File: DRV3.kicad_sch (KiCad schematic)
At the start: 15 parts

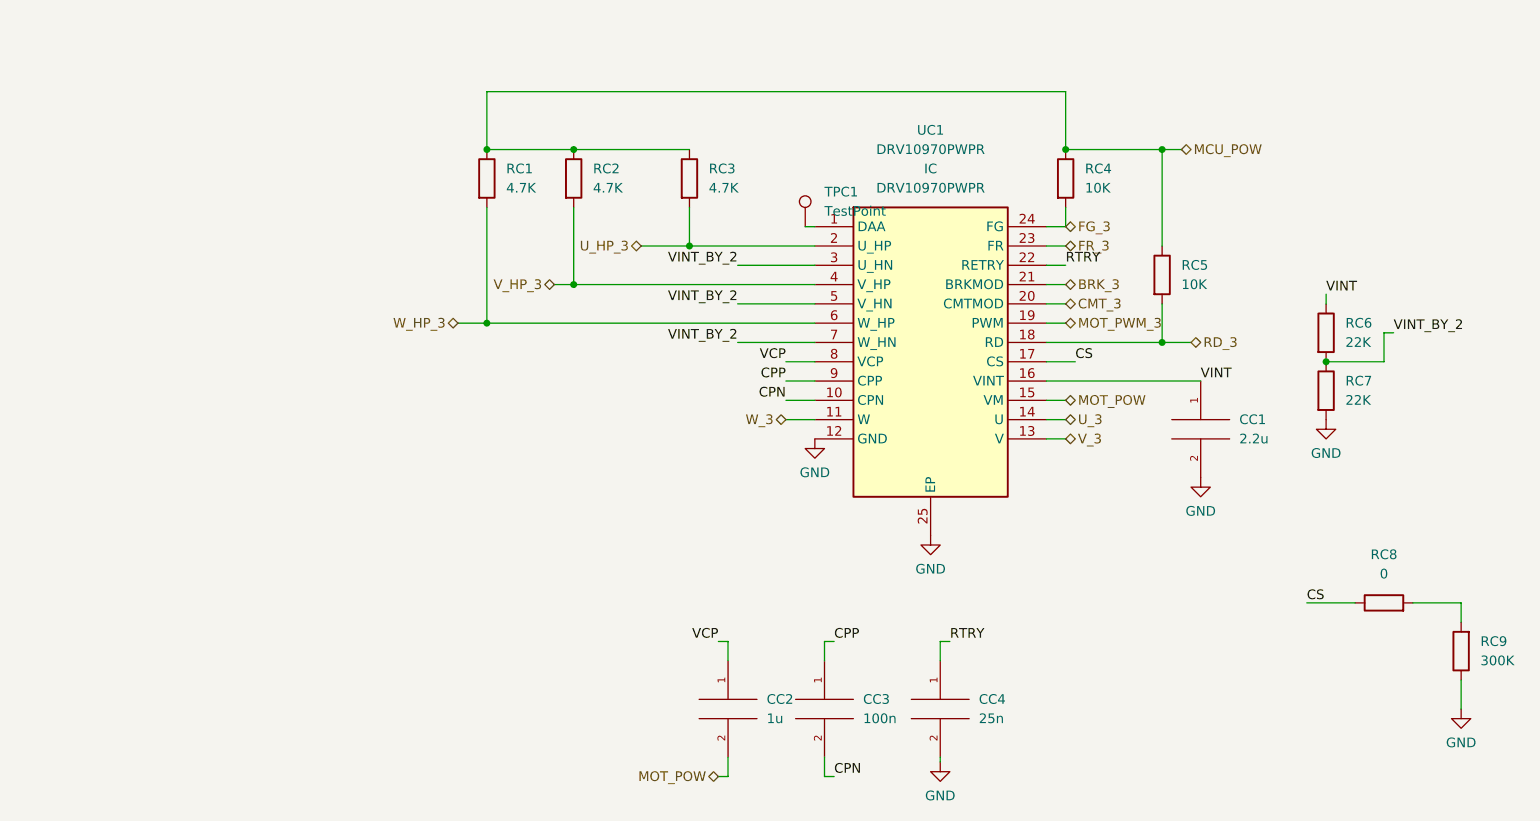
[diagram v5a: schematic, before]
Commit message: Page settings changed. Added some testpoints. Some comments are made.
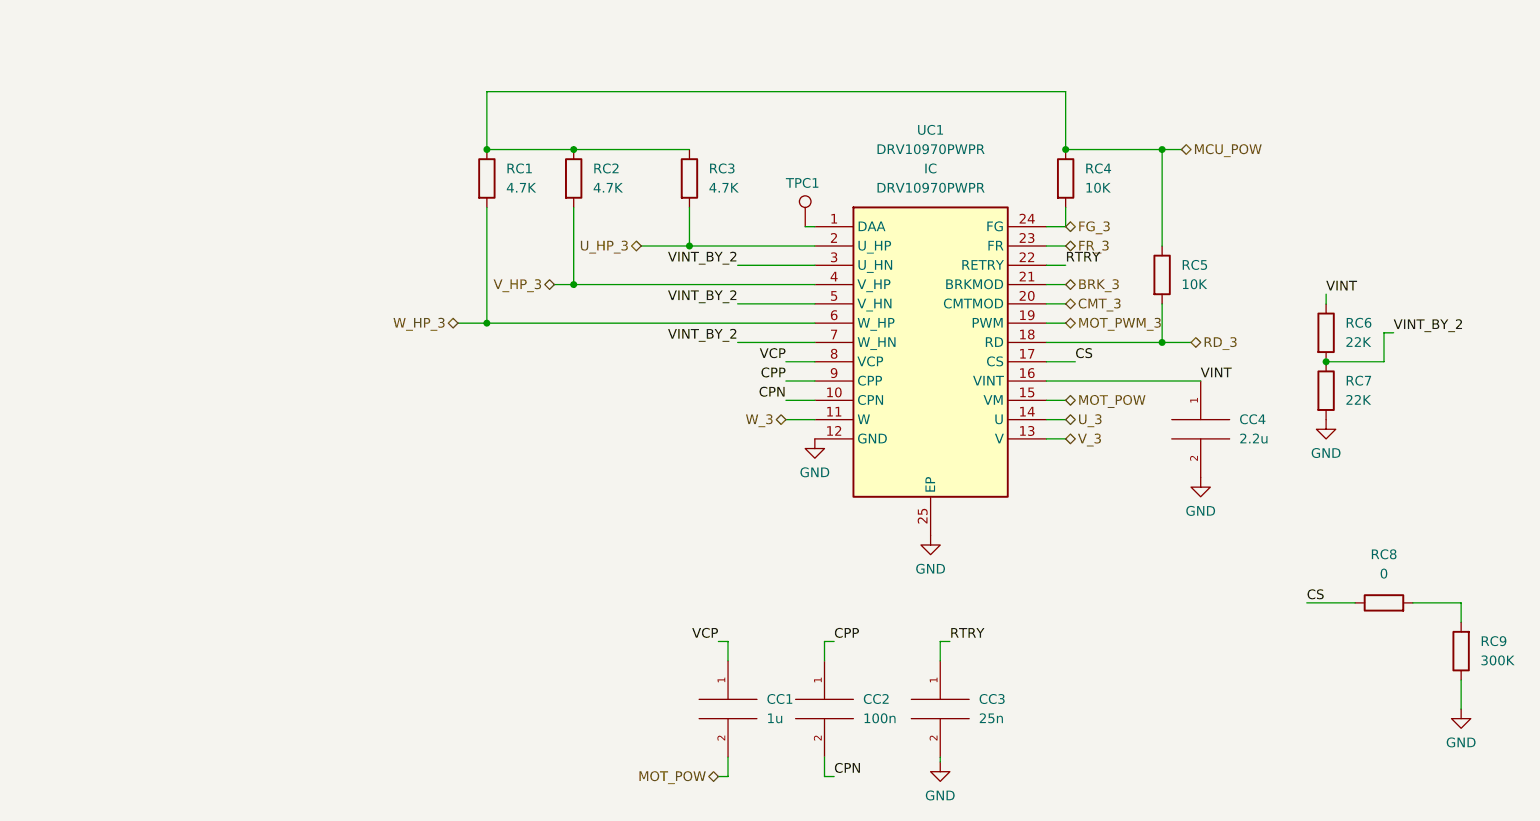
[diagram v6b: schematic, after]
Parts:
- TPC1: footprint (none) -> TestPoint:TestPoint_Plated_Hole_D2.0mm
- renumbered CC2 to CC1, CC3 to CC2, CC4 to CC3, CC1 to CC4
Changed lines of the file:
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@@
   (symbol (lib_id "upsat-comms-hardware:GND") (at 181.61 109.22 0) (unit 1)
     (in_bom yes) (on_board yes) (fields_autoplaced)
-    (property "Reference" "#PWR093" (id 0) (at 181.61 115.57 0)
+    (property "Reference" "#PWR0107" (id 0) (at 181.61 115.57 0)
       (effects (font (size 1.27 1.27)) hide)
     )
@@
   (symbol (lib_id "upsat-comms-hardware:GND") (at 130.81 104.14 0) (unit 1)
     (in_bom yes) (on_board yes) (fields_autoplaced)
-    (property "Reference" "#PWR092" (id 0) (at 130.81 110.49 0)
+    (property "Reference" "#PWR0104" (id 0) (at 130.81 110.49 0)
       (effects (font (size 1.27 1.27)) hide)
     )
@@
   (symbol (lib_id "pspice:C") (at 132.08 139.7 0) (unit 1)
     (in_bom yes) (on_board yes) (fields_autoplaced)
-    (property "Reference" "CC3" (id 0) (at 137.16 138.4299 0)
+    (property "Reference" "CC2" (id 0) (at 137.16 138.4299 0)
       (effects (font (size 1.27 1.27)) (justify left))
     )
@@
   (symbol (lib_id "upsat-comms-hardware:GND") (at 215.9 139.7 0) (unit 1)
     (in_bom yes) (on_board yes) (fields_autoplaced)
-    (property "Reference" "#PWR095" (id 0) (at 215.9 146.05 0)
+    (property "Reference" "#PWR0109" (id 0) (at 215.9 146.05 0)
       (effects (font (size 1.27 1.27)) hide)
     )
@@
     (pin "1")
   )
+  (symbol (lib_id "Connector:TestPoint") (at 129.54 76.2 0) (unit 1)
+    (in_bom yes) (on_board yes)
+    (property "Reference" "TPC1" (id 0) (at 127 70.485 0)
+      (effects (font (size 1.27 1.27)) (justify left))
+    )
+    (property "Value" "TestPoint" (id 1) (at 125.095 70.485 0)
+      (effects (font (size 1.27 1.27)) (justify left) hide)
+    )
+    (property "Footprint" "TestPoint:TestPoint_Plated_Hole_D2.0mm" (id 2) (at 134.62 76.2 0)
+      (effects (font (size 1.27 1.27)) hide)
+    )
+    (property "Datasheet" "~" (id 3) (at 134.62 76.2 0)
+      (effects (font (size 1.27 1.27)) hide)
+    )
+    (pin "1")
+  )
   (symbol (lib_id "pspice:C") (at 147.32 139.7 0) (unit 1)
     (in_bom yes) (on_board yes) (fields_autoplaced)
-    (property "Reference" "CC4" (id 0) (at 152.4 138.4299 0)
+    (property "Reference" "CC3" (id 0) (at 152.4 138.4299 0)
       (effects (font (size 1.27 1.27)) (justify left))
     )
@@
   (symbol (lib_id "pspice:C") (at 119.38 139.7 0) (unit 1)
     (in_bom yes) (on_board yes) (fields_autoplaced)
-    (property "Reference" "CC2" (id 0) (at 124.46 138.4299 0)
+    (property "Reference" "CC1" (id 0) (at 124.46 138.4299 0)
       (effects (font (size 1.27 1.27)) (justify left))
     )
@@
   (symbol (lib_id "upsat-comms-hardware:GND") (at 146.05 116.84 0) (unit 1)
     (in_bom yes) (on_board yes) (fields_autoplaced)
-    (property "Reference" "#PWR094" (id 0) (at 146.05 123.19 0)
+    (property "Reference" "#PWR0105" (id 0) (at 146.05 123.19 0)
       (effects (font (size 1.27 1.27)) hide)
     )
@@
   (symbol (lib_id "upsat-comms-hardware:GND") (at 198.12 101.6 0) (unit 1)
     (in_bom yes) (on_board yes) (fields_autoplaced)
-    (property "Reference" "#PWR091" (id 0) (at 198.12 107.95 0)
+    (property "Reference" "#PWR0108" (id 0) (at 198.12 107.95 0)
       (effects (font (size 1.27 1.27)) hide)
     )
@@
   (symbol (lib_id "upsat-comms-hardware:GND") (at 147.32 146.685 0) (unit 1)
     (in_bom yes) (on_board yes) (fields_autoplaced)
-    (property "Reference" "#PWR096" (id 0) (at 147.32 153.035 0)
+    (property "Reference" "#PWR0106" (id 0) (at 147.32 153.035 0)
       (effects (font (size 1.27 1.27)) hide)
     )
@@
     (property "Footprint" "" (id 2) (at 147.32 146.685 0))
     (property "Datasheet" "" (id 3) (at 147.32 146.685 0))
-    (pin "1")
-  )
-  (symbol (lib_id "Connector:TestPoint") (at 129.54 76.2 0) (unit 1)
-    (in_bom yes) (on_board yes) (fields_autoplaced)
-    (property "Reference" "TPC1" (id 0) (at 132.08 71.6279 0)
-      (effects (font (size 1.27 1.27)) (justify left))
-    )
-    (property "Value" "TestPoint" (id 1) (at 132.08 74.1679 0)
-      (effects (font (size 1.27 1.27)) (justify left))
-    )
-    (property "Footprint" "" (id 2) (at 134.62 76.2 0)
-      (effects (font (size 1.27 1.27)) hide)
-    )
-    (property "Datasheet" "~" (id 3) (at 134.62 76.2 0)
-      (effects (font (size 1.27 1.27)) hide)
-    )
     (pin "1")
   )
@@
   (symbol (lib_id "pspice:C") (at 181.61 102.87 0) (unit 1)
     (in_bom yes) (on_board yes) (fields_autoplaced)
-    (property "Reference" "CC1" (id 0) (at 186.69 101.5999 0)
-      (effects (font (size 1.27 1.27)) (justify left))
-    )
+    (property "Reference" "CC4" (id 0) (at 186.69 101.5999 0)
+      (effects (font (size 1.27 1.27)) (justify left))
+    )

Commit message: I2C lines are pulled up
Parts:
- CC1, CC2, CC3, CC4: footprint (none) -> Capacitor_SMD:C_0603_1608Metric
- RC1, RC2, RC3, RC4, RC5, RC6, RC7, RC8, RC9: footprint (none) -> Resistor_SMD:R_0603_1608Metric
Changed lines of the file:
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@@
     (property "Reference" "RC8" (id 0) (at 205.74 119.38 90))
     (property "Value" "0" (id 1) (at 205.74 121.92 90))
-    (property "Footprint" "" (id 2) (at 205.74 127.508 90)
+    (property "Footprint" "Resistor_SMD:R_0603_1608Metric" (id 2) (at 205.74 127.508 90)
       (effects (font (size 1.27 1.27)) hide)
     )
@@
       (effects (font (size 1.27 1.27)) (justify left))
     )
-    (property "Footprint" "" (id 2) (at 174.752 82.55 90)
+    (property "Footprint" "Resistor_SMD:R_0603_1608Metric" (id 2) (at 174.752 82.55 90)
       (effects (font (size 1.27 1.27)) hide)
     )
@@
       (effects (font (size 1.27 1.27)) (justify left))
     )
-    (property "Footprint" "" (id 2) (at 162.052 69.85 90)
+    (property "Footprint" "Resistor_SMD:R_0603_1608Metric" (id 2) (at 162.052 69.85 90)
       (effects (font (size 1.27 1.27)) hide)
     )
@@
       (effects (font (size 1.27 1.27)) (justify left))
     )
-    (property "Footprint" "" (id 2) (at 97.282 69.85 90)
+    (property "Footprint" "Resistor_SMD:R_0603_1608Metric" (id 2) (at 97.282 69.85 90)
       (effects (font (size 1.27 1.27)) hide)
     )
@@
   (symbol (lib_id "upsat-comms-hardware:GND") (at 181.61 109.22 0) (unit 1)
     (in_bom yes) (on_board yes) (fields_autoplaced)
-    (property "Reference" "#PWR0107" (id 0) (at 181.61 115.57 0)
+    (property "Reference" "#PWR0108" (id 0) (at 181.61 115.57 0)
       (effects (font (size 1.27 1.27)) hide)
     )
@@
       (effects (font (size 1.27 1.27)) (justify right))
     )
-    (property "Footprint" "" (id 2) (at 217.678 132.08 90)
+    (property "Footprint" "Resistor_SMD:R_0603_1608Metric" (id 2) (at 217.678 132.08 90)
       (effects (font (size 1.27 1.27)) hide)
     )
@@
   (symbol (lib_id "upsat-comms-hardware:GND") (at 130.81 104.14 0) (unit 1)
     (in_bom yes) (on_board yes) (fields_autoplaced)
-    (property "Reference" "#PWR0104" (id 0) (at 130.81 110.49 0)
+    (property "Reference" "#PWR0105" (id 0) (at 130.81 110.49 0)
       (effects (font (size 1.27 1.27)) hide)
     )
@@
       (effects (font (size 1.27 1.27)) (justify left))
     )
-    (property "Footprint" "" (id 2) (at 112.522 69.85 90)
+    (property "Footprint" "Resistor_SMD:R_0603_1608Metric" (id 2) (at 112.522 69.85 90)
       (effects (font (size 1.27 1.27)) hide)
     )
@@
       (effects (font (size 1.27 1.27)) (justify left))
     )
-    (property "Footprint" "" (id 2) (at 132.08 139.7 0)
+    (property "Footprint" "Capacitor_SMD:C_0603_1608Metric" (id 2) (at 132.08 139.7 0)
       (effects (font (size 1.27 1.27)) hide)
     )
@@
   (symbol (lib_id "upsat-comms-hardware:GND") (at 215.9 139.7 0) (unit 1)
     (in_bom yes) (on_board yes) (fields_autoplaced)
-    (property "Reference" "#PWR0109" (id 0) (at 215.9 146.05 0)
+    (property "Reference" "#PWR0110" (id 0) (at 215.9 146.05 0)
       (effects (font (size 1.27 1.27)) hide)
     )
@@
       (effects (font (size 1.27 1.27)) (justify left))
     )
-    (property "Footprint" "" (id 2) (at 147.32 139.7 0)
+    (property "Footprint" "Capacitor_SMD:C_0603_1608Metric" (id 2) (at 147.32 139.7 0)
       (effects (font (size 1.27 1.27)) hide)
     )
@@
       (effects (font (size 1.27 1.27)) (justify left))
     )
-    (property "Footprint" "" (id 2) (at 196.342 90.17 90)
+    (property "Footprint" "Resistor_SMD:R_0603_1608Metric" (id 2) (at 196.342 90.17 90)
       (effects (font (size 1.27 1.27)) hide)
     )
@@
       (effects (font (size 1.27 1.27)) (justify left))
     )
-    (property "Footprint" "" (id 2) (at 119.38 139.7 0)
+    (property "Footprint" "Capacitor_SMD:C_0603_1608Metric" (id 2) (at 119.38 139.7 0)
       (effects (font (size 1.27 1.27)) hide)
     )
@@
   (symbol (lib_id "upsat-comms-hardware:GND") (at 146.05 116.84 0) (unit 1)
     (in_bom yes) (on_board yes) (fields_autoplaced)
-    (property "Reference" "#PWR0105" (id 0) (at 146.05 123.19 0)
+    (property "Reference" "#PWR0106" (id 0) (at 146.05 123.19 0)
       (effects (font (size 1.27 1.27)) hide)
     )
@@
   (symbol (lib_id "upsat-comms-hardware:GND") (at 198.12 101.6 0) (unit 1)
     (in_bom yes) (on_board yes) (fields_autoplaced)
-    (property "Reference" "#PWR0108" (id 0) (at 198.12 107.95 0)
+    (property "Reference" "#PWR0109" (id 0) (at 198.12 107.95 0)
       (effects (font (size 1.27 1.27)) hide)
     )
@@
       (effects (font (size 1.27 1.27)) (justify left))
     )
-    (property "Footprint" "" (id 2) (at 85.852 69.85 90)
+    (property "Footprint" "Resistor_SMD:R_0603_1608Metric" (id 2) (at 85.852 69.85 90)
       (effects (font (size 1.27 1.27)) hide)
     )
@@
   (symbol (lib_id "upsat-comms-hardware:GND") (at 147.32 146.685 0) (unit 1)
     (in_bom yes) (on_board yes) (fields_autoplaced)
-    (property "Reference" "#PWR0106" (id 0) (at 147.32 153.035 0)
+    (property "Reference" "#PWR0107" (id 0) (at 147.32 153.035 0)
       (effects (font (size 1.27 1.27)) hide)
     )
@@
       (effects (font (size 1.27 1.27)) (justify left))
     )
-    (property "Footprint" "" (id 2) (at 181.61 102.87 0)
+    (property "Footprint" "Capacitor_SMD:C_0603_1608Metric" (id 2) (at 181.61 102.87 0)
       (effects (font (size 1.27 1.27)) hide)
     )
@@
       (effects (font (size 1.27 1.27)) (justify left))
     )
-    (property "Footprint" "" (id 2) (at 196.342 97.79 90)
-      (effects (font (size 1.27 1.27)) hide)
-    )
+    (property "Footprint" "Resistor_SMD:R_0603_1608Metric" (id 2) (at 196.342 97.79 90)
+      (effects (font (size 1.27 1.27)) hide)
+    )

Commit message: Final Schematic
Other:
- note added: "A low-ESR ceramic capacitor must be placed in between the VM and VCP pins. TI recommends a value of 1-µF rated for 16 V. Place this component as close as possible to the pins."
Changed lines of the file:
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@@
     (stroke (width 0) (type default) (color 0 0 0 0))
+  )
+  (text "A low-ESR ceramic capacitor must be placed in between the VM and VCP pins. TI recommends a value of 1-µF\nrated for 16 V. Place this component as close as possible to the pins."
+    (at 91.44 52.705 0)
+    (effects (font (size 1.27 1.27) (thickness 0.254) bold italic) (justify left bottom))
   )
   (label "CS" (at 165.1 93.98 0)
